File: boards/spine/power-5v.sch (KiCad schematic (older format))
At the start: 15 parts, among them U8 RT8299A

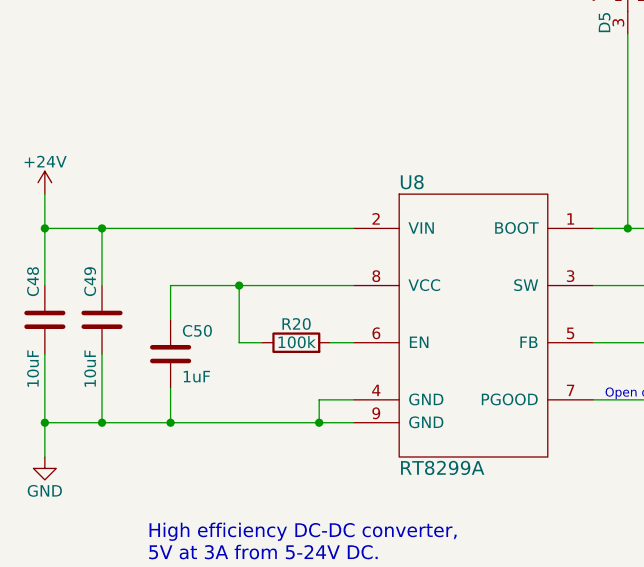
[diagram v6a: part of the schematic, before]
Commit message: BOM tweaks, starting DC/DC fixes
VCC is not active until EN goes high, so EN must be
connected to VIN via the 100k resistor. Internal resistance
is 5k to a 3V zener.
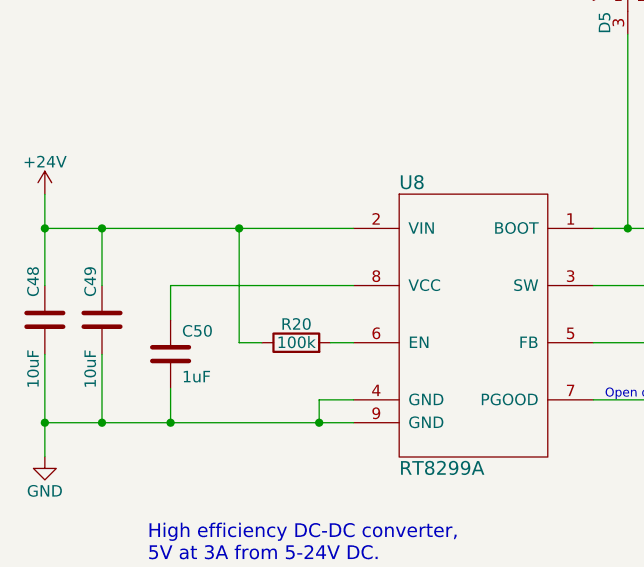
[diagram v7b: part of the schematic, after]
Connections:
- net +24V: now also R20.1
- net at C50.1, U8.8 (VCC): no longer R20.1
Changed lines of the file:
@@
 Wire Wire Line
 	5350 3800 5600 3800
-Connection ~ 3100 4050
-Wire Wire Line
-	3100 4300 3100 4050
 Wire Wire Line
 	3200 4300 3100 4300
@@
 Text Notes 2700 5650 0    60   ~ 0
 High efficiency DC-DC converter,\n5V at 3A from 5-24V DC.\n\nThis 5V rail is shared by the USB output (up to 2A),\nthe modules (100mA each), and all FPGA and USB\ncontroller power rails.
+Wire Wire Line
+	3100 4300 3100 3800
+Connection ~ 3100 3800
 $EndSCHEMATC

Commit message: BOM cleanup
Especially fix the confusing and mostly incorrect Mfg/Mfr stuff that I inherited from somewhere.
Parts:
- C48, C49, C53, C54: Mfg1 (none) -> Murata; Mfg1Id (none) -> GRM31CR61H106MA12L; MfgId GRM31CR61H106MA12L -> (none); MfrId Murata -> (none)
- C50: Mfg1 (none) -> Murata; Mfg1Id (none) -> GRM219R61H105KA73D; MfgId GRM219R61H105KA73D -> (none); MfrId Murata -> (none)
- C51: Mfg1 (none) -> Murata; Mfg1Id (none) -> GRM21BR71H104MA01L; MfgId GRM21BR71H104MA01L -> (none); MfrId Murata -> (none)
- C52: Mfg1 (none) -> Murata; Mfg1Id (none) -> GRM2165C1H101JA01D; MfgId GRM2165C1H101JA01D -> (none); MfrId Murata -> (none)
- D5: Mfg1 (none) -> Diodes Inc; Mfg1Id (none) -> BAT54C-7-F; MfgId BAT54C-7-F -> (none); MfrId Diodes Inc -> (none)
- L1: Mfg1 (none) -> Bourns; Mfg1Id (none) -> SRR1280-220M; MfgId Bourns -> (none); MfrId SRR1280-220M -> (none)
- R20, R24: Mfg1 (none) -> Stackpole; Mfg1Id (none) -> RMCF0805JT100K; MfgId RMCF0805JT100K -> (none); MfrId Stackpole -> (none)
- R21: Mfg1 (none) -> Stackpole; Mfg1Id (none) -> RMCF0805JT150R; MfgId RMCF0805JT150R -> (none); MfrId Stackpole -> (none)
- R22: Mfg1 (none) -> Stackpole; Mfg1Id (none) -> RMCF0805FT27K0; MfgId RMCF0805FT27K0 -> (none); MfrId Stackpole -> (none)
- R23: Mfg1 (none) -> Stackpole; Mfg1Id (none) -> RMCF0805FT5K10; MfgId RMCF0805FT5K10 -> (none); MfrId Stackpole -> (none)
- U8: Mfg1 (none) -> Richtek; Mfg1Id (none) -> RT8299AZSP; MfgId RT8299AZSP -> (none); MfrId Richtek -> (none)
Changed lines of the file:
@@
 F 3 "https://www.seielect.com/Catalog/SEI-RMCF_RMCP.pdf" H 3350 4300 30  0001 C CNN
 F 4 "Digikey" V 3350 4300 60  0001 C CNN "Vend1"
-F 5 "Stackpole" V 3350 4300 60  0001 C CNN "MfrId"
-F 6 "RMCF0805JT100K" V 3350 4300 60  0001 C CNN "MfgId"
+F 5 "Stackpole" V 3350 4300 60  0001 C CNN "Mfg1"
+F 6 "RMCF0805JT100K" V 3350 4300 60  0001 C CNN "Mfg1Id"
 F 7 "RMCF0805JT100KCT-ND" V 3350 4300 60  0001 C CNN "Vend1Id"
 F 8 "0.00320" V 3350 4300 60  0001 C CNN "RefPrice1k"
@@
 F 2 "Capacitors_SMD:C_1206" H 2288 4050 30  0001 C CNN
 F 3 "http://www.murata.com/~/media/webrenewal/support/library/catalog/products/capacitor/mlcc/c02e.ashx" H 2250 4200 60  0001 C CNN
-F 4 "GRM31CR61H106MA12L" H 2300 4000 39  0001 L BNN "MfgId"
-F 5 "Murata" H 2250 4200 60  0001 C CNN "MfrId"
+F 4 "GRM31CR61H106MA12L" H 2300 4000 39  0001 L BNN "Mfg1Id"
+F 5 "Murata" H 2250 4200 60  0001 C CNN "Mfg1"
 F 6 "Digikey" H 2250 4200 60  0001 C CNN "Vend1"
 F 7 "490-10756-2-ND" H 2250 4200 60  0001 C CNN "Vend1Id"
@@
 F 2 "Capacitors_SMD:C_0805" H 2838 4200 30  0001 C CNN
 F 3 "http://www.murata.com/~/media/webrenewal/support/library/catalog/products/capacitor/mlcc/c02e.ashx" H 2800 4350 60  0001 C CNN
-F 4 "GRM219R61H105KA73D" H 2850 4150 39  0001 L BNN "MfgId"
-F 5 "Murata" H 2800 4350 60  0001 C CNN "MfrId"
+F 4 "GRM219R61H105KA73D" H 2850 4150 39  0001 L BNN "Mfg1Id"
+F 5 "Murata" H 2800 4350 60  0001 C CNN "Mfg1"
 F 6 "Digikey" H 2800 4350 60  0001 C CNN "Vend1"
 F 7 "490-10743-2-ND" H 2800 4350 60  0001 C CNN "Vend1Id"
@@
 F 4 "Digikey" H 4050 3600 60  0001 C CNN "Vend1"
 F 5 "1028-1295-1-ND" H 4050 3600 60  0001 C CNN "Vend1Id"
-F 6 "Richtek" H 4050 3600 60  0001 C CNN "MfrId"
-F 7 "RT8299AZSP" H 4050 3600 60  0001 C CNN "MfgId"
+F 6 "Richtek" H 4050 3600 60  0001 C CNN "Mfg1"
+F 7 "RT8299AZSP" H 4050 3600 60  0001 C CNN "Mfg1Id"
 F 8 "0.37752" H 4050 3600 60  0001 C CNN "RefPrice1k"
 	1    4050 3600
@@
 F 5 "490-9672-2-ND" V 5200 3800 60  0001 C CNN "Vend1Id"
 F 6 "Digikey" V 5200 3800 60  0001 C CNN "Vend1"
-F 7 "Murata" V 5200 3800 60  0001 C CNN "MfrId"
-F 8 "GRM21BR71H104MA01L" V 5200 3800 60  0001 C CNN "MfgId"
+F 7 "Murata" V 5200 3800 60  0001 C CNN "Mfg1"
+F 8 "GRM21BR71H104MA01L" V 5200 3800 60  0001 C CNN "Mfg1Id"
 	1    5200 3800
 	0    1    1    0
@@
 F 3 "http://www.bourns.com/docs/Product-Datasheets/SRR1280.pdf" H 5600 3250 60  0001 C CNN
 F 4 "SRR1280-220MTR-ND" V 5600 3250 60  0001 C CNN "Vend1Id"
-F 5 "Bourns" V 5600 3250 60  0001 C CNN "MfgId"
-F 6 "SRR1280-220M" V 5600 3250 60  0001 C CNN "MfrId"
+F 5 "Bourns" V 5600 3250 60  0001 C CNN "Mfg1"
+F 6 "SRR1280-220M" V 5600 3250 60  0001 C CNN "Mfg1Id"
 F 7 "Digikey" V 5600 3250 60  0001 C CNN "Vend1"
 F 8 "0.42160" V 5600 3250 60  0001 C CNN "RefPrice1k"
@@
 F 5 "RMCF0805JT150RCT-ND" V 5600 4900 60  0001 C CNN "Vend1Id"
 F 6 "Digikey" V 5600 4900 60  0001 C CNN "Vend1"
-F 7 "Stackpole" V 5600 4900 60  0001 C CNN "MfrId"
-F 8 "RMCF0805JT150R" V 5600 4900 60  0001 C CNN "MfgId"
+F 7 "Stackpole" V 5600 4900 60  0001 C CNN "Mfg1"
+F 8 "RMCF0805JT150R" V 5600 4900 60  0001 C CNN "Mfg1Id"
 	1    5600 4900
 	-1   0    0    1
@@
 F 5 "490-1615-1-ND" V 5600 5200 60  0001 C CNN "Vend1Id"
 F 6 "Digikey" V 5600 5200 60  0001 C CNN "Vend1"
-F 7 "Murata" V 5600 5200 60  0001 C CNN "MfrId"
-F 8 "GRM2165C1H101JA01D" V 5600 5200 60  0001 C CNN "MfgId"
+F 7 "Murata" V 5600 5200 60  0001 C CNN "Mfg1"
+F 8 "GRM2165C1H101JA01D" V 5600 5200 60  0001 C CNN "Mfg1Id"
 	1    5600 5200
 	-1   0    0    1
@@
 F 2 "Capacitors_SMD:C_1206" H 2538 4050 30  0001 C CNN
 F 3 "http://www.murata.com/~/media/webrenewal/support/library/catalog/products/capacitor/mlcc/c02e.ashx" H 2500 4200 60  0001 C CNN
-F 4 "GRM31CR61H106MA12L" H 2550 4000 39  0001 L BNN "MfgId"
-F 5 "Murata" H 2500 4200 60  0001 C CNN "MfrId"
+F 4 "GRM31CR61H106MA12L" H 2550 4000 39  0001 L BNN "Mfg1Id"
+F 5 "Murata" H 2500 4200 60  0001 C CNN "Mfg1"
 F 6 "Digikey" H 2500 4200 60  0001 C CNN "Vend1"
 F 7 "490-10756-2-ND" H 2500 4200 60  0001 C CNN "Vend1Id"
@@
 F 2 "Capacitors_SMD:C_1206" H 7238 2900 30  0001 C CNN
 F 3 "http://www.murata.com/~/media/webrenewal/support/library/catalog/products/capacitor/mlcc/c02e.ashx" H 7200 3050 60  0001 C CNN
-F 4 "GRM31CR61H106MA12L" H 7250 2850 39  0001 L BNN "MfgId"
-F 5 "Murata" H 7200 3050 60  0001 C CNN "MfrId"
+F 4 "GRM31CR61H106MA12L" H 7250 2850 39  0001 L BNN "Mfg1Id"
+F 5 "Murata" H 7200 3050 60  0001 C CNN "Mfg1"
 F 6 "Digikey" H 7200 3050 60  0001 C CNN "Vend1"
 F 7 "490-10756-2-ND" H 7200 3050 60  0001 C CNN "Vend1Id"
@@
 F 2 "Capacitors_SMD:C_1206" H 7488 2900 30  0001 C CNN
 F 3 "http://www.murata.com/~/media/webrenewal/support/library/catalog/products/capacitor/mlcc/c02e.ashx" H 7450 3050 60  0001 C CNN
-F 4 "GRM31CR61H106MA12L" H 7500 2850 39  0001 L BNN "MfgId"
-F 5 "Murata" H 7450 3050 60  0001 C CNN "MfrId"
+F 4 "GRM31CR61H106MA12L" H 7500 2850 39  0001 L BNN "Mfg1Id"
+F 5 "Murata" H 7450 3050 60  0001 C CNN "Mfg1"
 F 6 "Digikey" H 7450 3050 60  0001 C CNN "Vend1"
 F 7 "490-10756-2-ND" H 7450 3050 60  0001 C CNN "Vend1Id"
@@
 F 3 "https://www.seielect.com/Catalog/SEI-RMCF_RMCP.pdf" H 6250 4900 30  0001 C CNN
 F 4 "Digikey" V 6250 4900 60  0001 C CNN "Vend1"
-F 5 "Stackpole" V 6250 4900 60  0001 C CNN "MfrId"
-F 6 "RMCF0805FT5K10" V 6250 4900 60  0001 C CNN "MfgId"
+F 5 "Stackpole" V 6250 4900 60  0001 C CNN "Mfg1"
+F 6 "RMCF0805FT5K10" V 6250 4900 60  0001 C CNN "Mfg1Id"
 F 7 "RMCF0805FT5K10CT-ND" V 6250 4900 60  0001 C CNN "Vend1Id"
 F 8 "0.00448" V 6250 4900 60  0001 C CNN "RefPrice1k"
@@
 F 3 "https://www.seielect.com/Catalog/SEI-RMCF_RMCP.pdf" H 6250 4000 30  0001 C CNN
 F 4 "Digikey" V 6250 4000 60  0001 C CNN "Vend1"
-F 5 "Stackpole" V 6250 4000 60  0001 C CNN "MfrId"
-F 6 "RMCF0805FT27K0" V 6250 4000 60  0001 C CNN "MfgId"
+F 5 "Stackpole" V 6250 4000 60  0001 C CNN "Mfg1"
+F 6 "RMCF0805FT27K0" V 6250 4000 60  0001 C CNN "Mfg1Id"
 F 7 "RMCF0805FT27K0CT-ND" V 6250 4000 60  0001 C CNN "Vend1Id"
 F 8 "0.00448" V 6250 4000 60  0001 C CNN "RefPrice1k"
@@
 F 3 "https://www.seielect.com/Catalog/SEI-RMCF_RMCP.pdf" H 6650 4000 30  0001 C CNN
 F 4 "Digikey" V 6650 4000 60  0001 C CNN "Vend1"
-F 5 "Stackpole" V 6650 4000 60  0001 C CNN "MfrId"
-F 6 "RMCF0805JT100K" V 6650 4000 60  0001 C CNN "MfgId"
+F 5 "Stackpole" V 6650 4000 60  0001 C CNN "Mfg1"
+F 6 "RMCF0805JT100K" V 6650 4000 60  0001 C CNN "Mfg1Id"
 F 7 "RMCF0805JT100KCT-ND" V 6650 4000 60  0001 C CNN "Vend1Id"
 F 8 "0.00320" V 6650 4000 60  0001 C CNN "RefPrice1k"
@@
 F 2 "TO_SOT_Packages_SMD:SOT-23" H 4800 2750 60  0001 C CNN
 F 3 "http://www.diodes.com/_files/datasheets/ds11005.pdf" H 4800 2750 60  0001 C CNN
-F 4 "Diodes Inc" H 4800 2900 39  0001 C CNN "MfrId"
-F 5 "BAT54C-7-F" H 4800 2850 39  0000 C CNN "MfgId"
+F 4 "Diodes Inc" H 4800 2900 39  0001 C CNN "Mfg1"
+F 5 "BAT54C-7-F" H 4800 2850 39  0000 C CNN "Mfg1Id"
 F 6 "BAT54C-FDICT-ND" V 4800 2750 60  0001 C CNN "Vend1Id"
 F 7 ".03955" V 4800 2750 60  0001 C CNN "RefPrice1k"
@@
 72 0F 1C A9 DC 70 49 CB 79 33 88 85 99 AD 01 6C 4B 10 FC 3B 13 DE 3B 37 68 79 AD 07 BC 00 3C 0E
 3C 31 EE E3 D8 E7 0F 03 D7 7B 9F FB C1 E1 FF 01 18 C4 96 1D B8 0E 40 07 00 00 00 00 49 45 4E 44
-AE 42 60 82 FF
+AE 42 60 82 B0
 EndData
 $EndBitmap
